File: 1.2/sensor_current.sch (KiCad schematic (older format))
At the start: 19 parts, among them U1 TL084, U2 AD8226

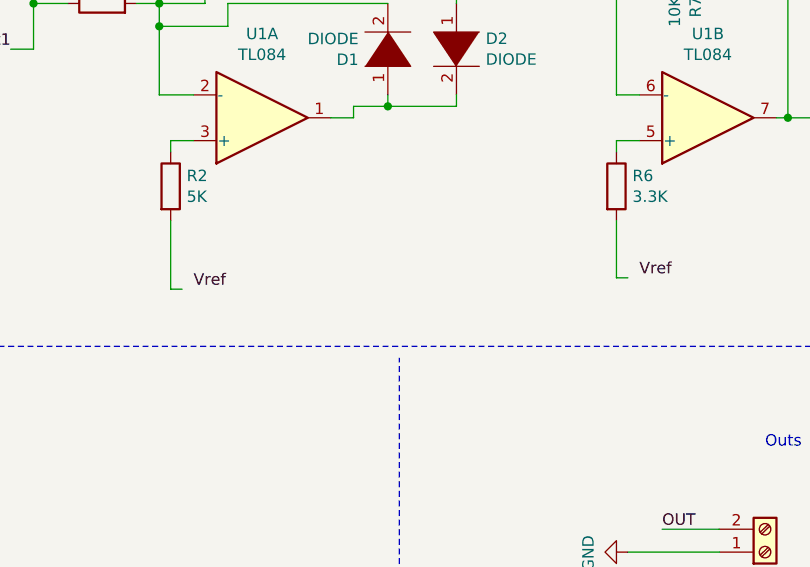
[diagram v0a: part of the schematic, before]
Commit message: error fixed
missing conection detected and eliminated
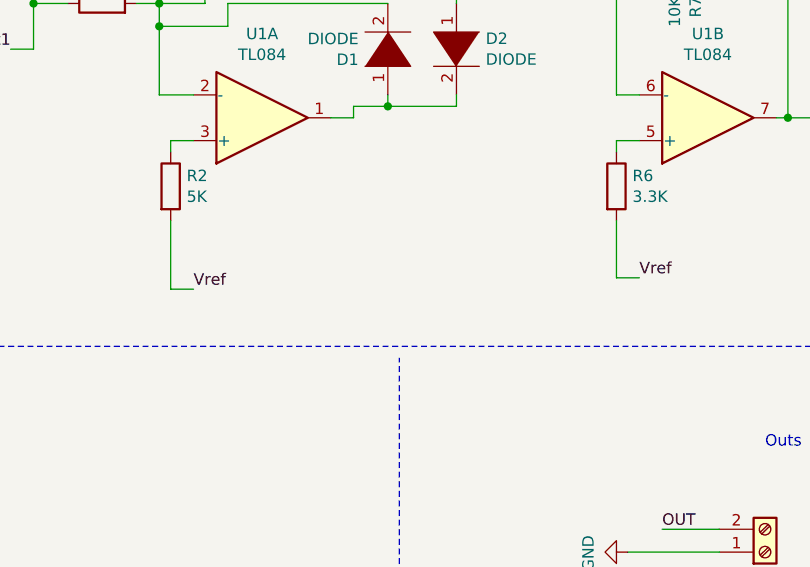
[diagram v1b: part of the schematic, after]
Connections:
- net Vref: now also R2.2, R6.2
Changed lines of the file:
@@
 Vref
 Wire Wire Line
-	9250 2850 9200 2850
-Wire Wire Line
 	9200 2850 9200 2600
-Wire Wire Line
-	7300 2900 7250 2900
 Wire Wire Line
 	7250 2600 7250 2900
@@
 	1    0    0    1
 $EndComp
+Wire Wire Line
+	7250 2900 7350 2900
+Wire Wire Line
+	9200 2850 9300 2850
 $EndSCHEMATC
